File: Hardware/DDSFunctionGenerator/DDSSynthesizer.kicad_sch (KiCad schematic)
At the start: 46 parts, among them J5 Conn_Coaxial, J6 Conn_Coaxial, U1 TC1107-3.3VOA, U4 AD9832, X1 XO91

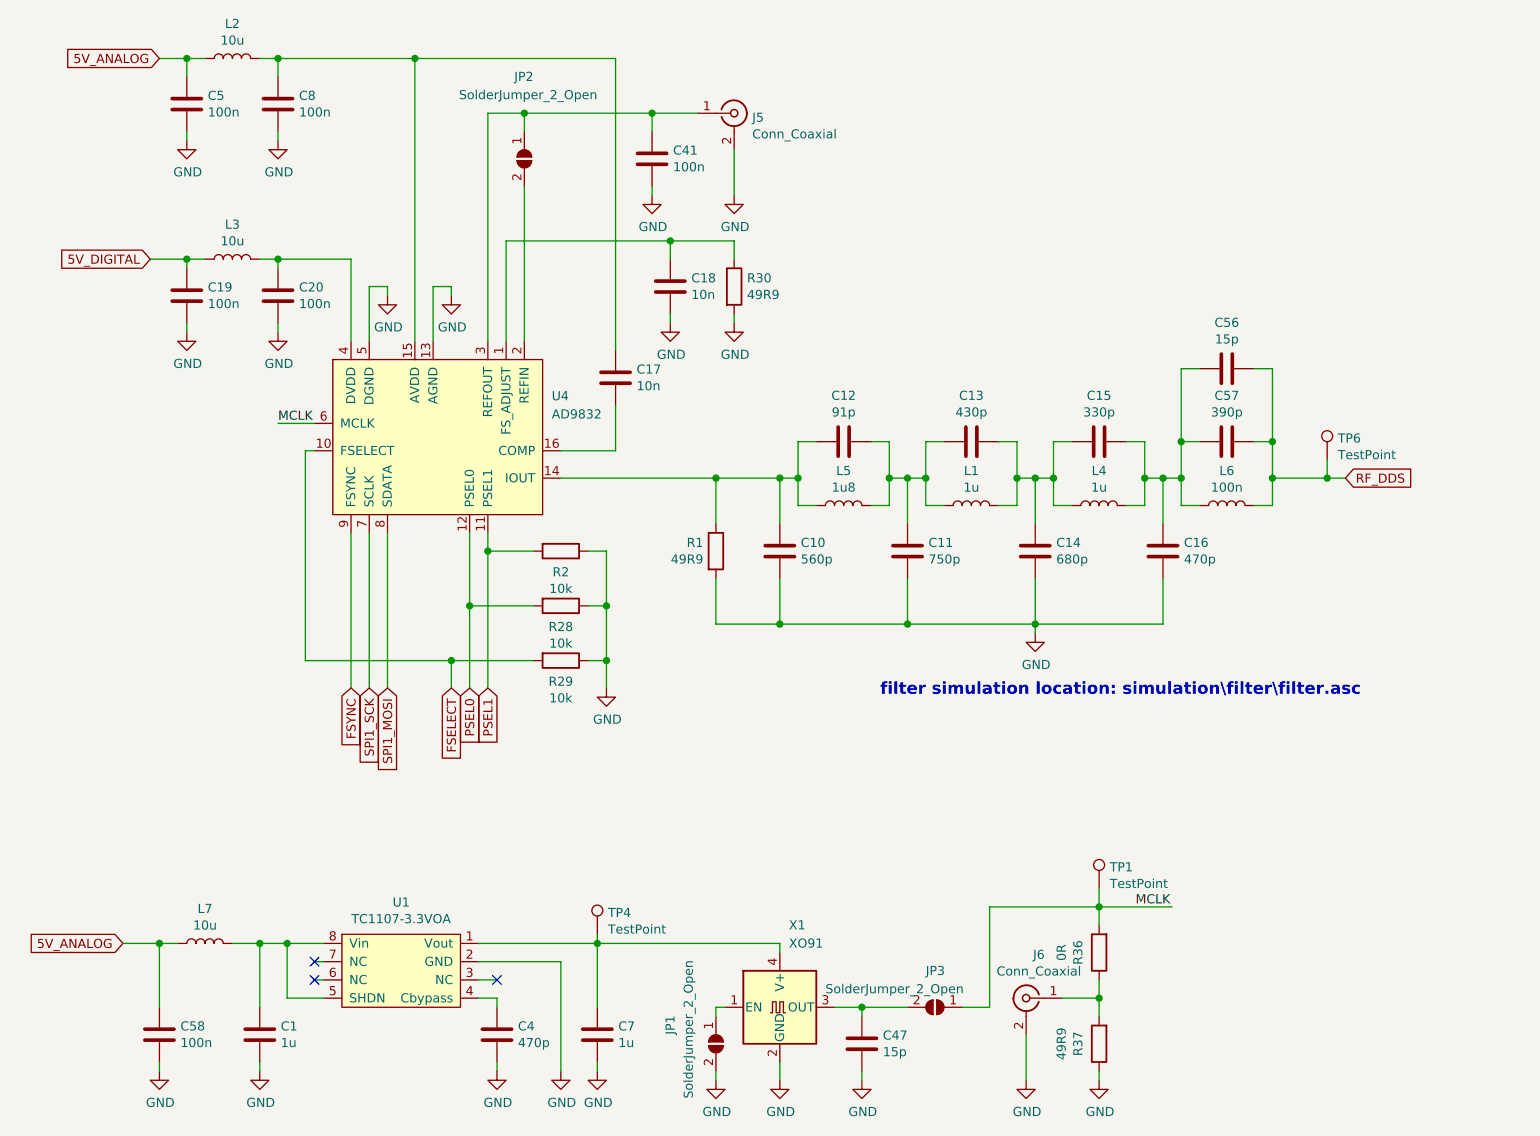
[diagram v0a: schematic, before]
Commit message: move to raspbbery pico, first draft
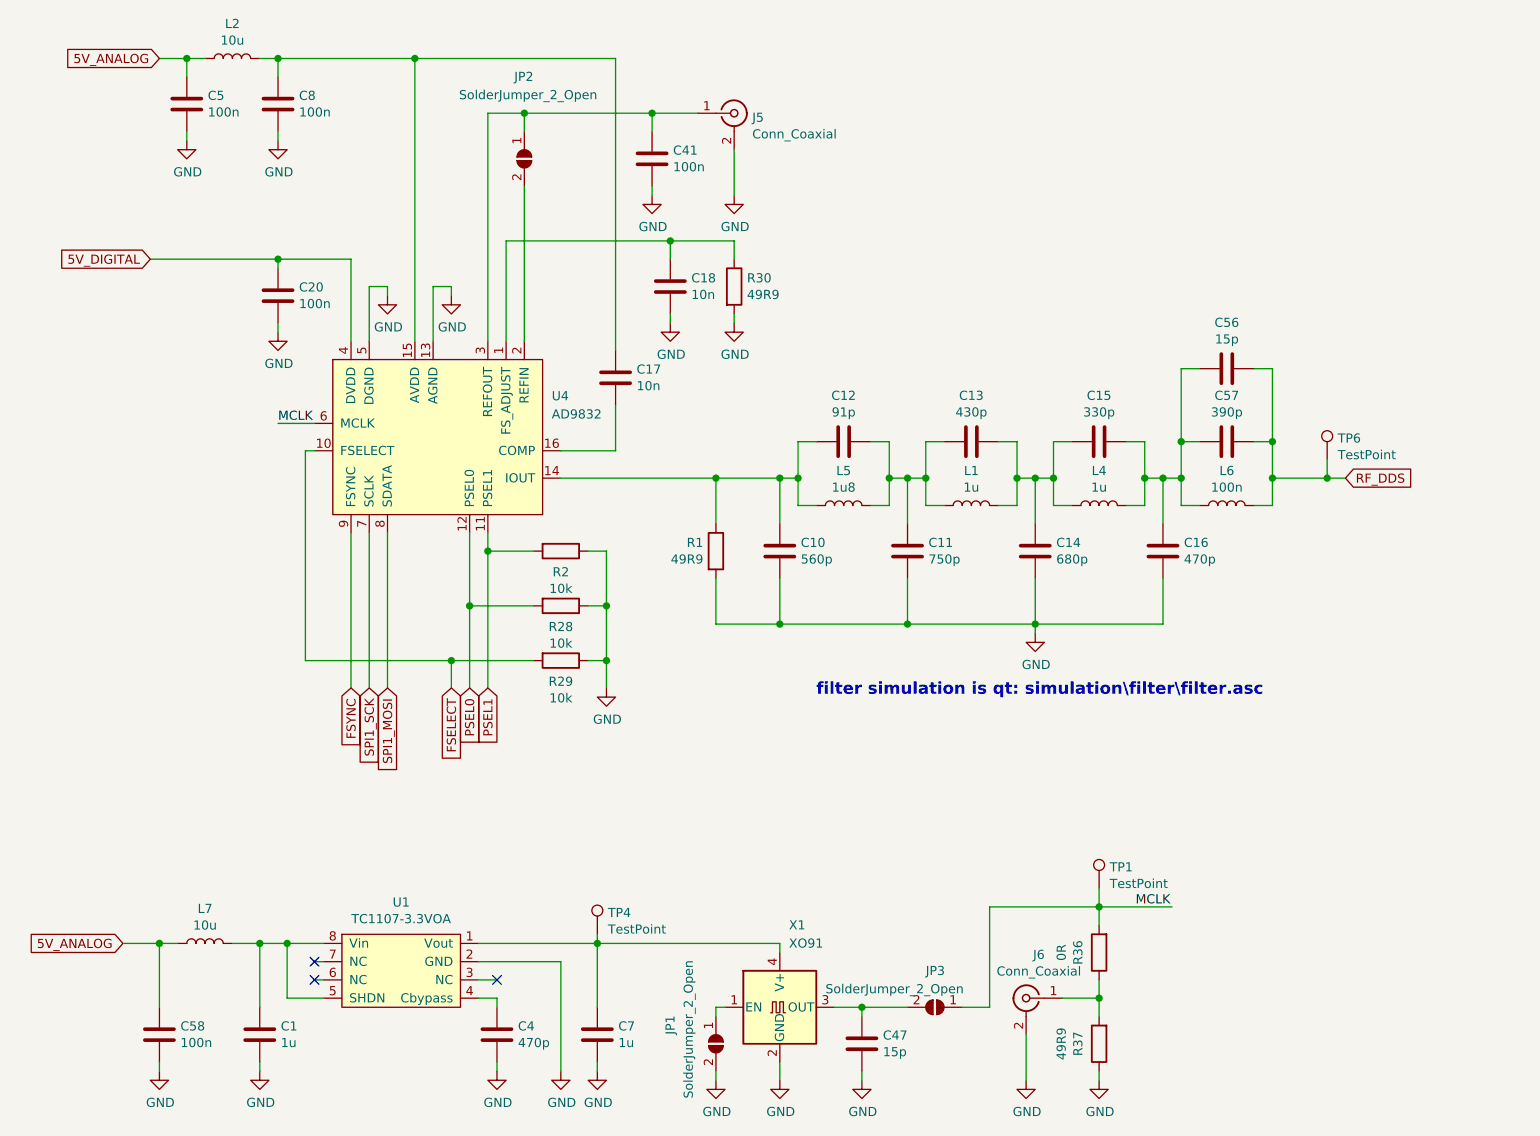
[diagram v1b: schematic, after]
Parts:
- removed C19: 100n, Capacitor_SMD:C_0402_1005Metric, symbol Device:C
- removed L3: 10u, Inductor_SMD:L_0805_2012Metric, symbol Device:L
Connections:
- net 5V_DIGITAL: now also C20.1, U4.4 (DVDD)
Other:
- note added: "filter simulation is qt: simulation\filter\filter.asc"
- note removed: "filter simulation location: simulation\filter\filter.asc"
